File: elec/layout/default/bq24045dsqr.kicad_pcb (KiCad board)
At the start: 2 copper layers, 4 parts

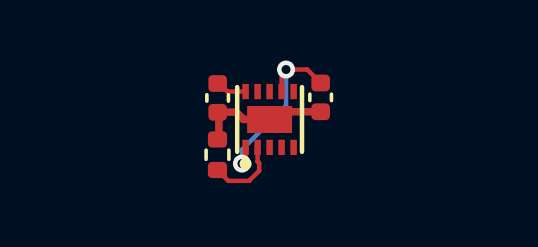
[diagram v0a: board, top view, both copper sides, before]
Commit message: updated to newest ato syntax, rearanged equations for solver
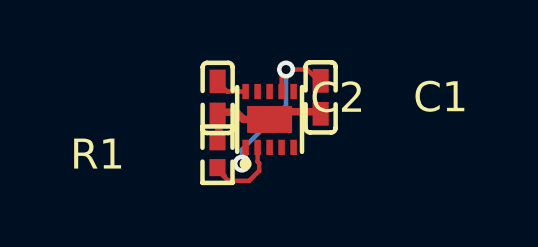
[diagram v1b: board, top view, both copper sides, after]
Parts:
- C1, C2: value 25V 1uF X5R ±10% 0402 Multilayer Ceramic Capacitors MLCC - SMD/SMT ROHS -> 1µF ±10% 25V X5R; footprint lib:C0402 -> atopile:C0402-b3ef17
- R1: value 100mW Thick Film Resistors ±100ppm/℃ ±1% 604Ω 0402 Chip Resistor - Surface Mount ROHS -> 560Ω ±1% 62.5mW; footprint lib:R0402 -> atopile:R0402-56259e
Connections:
- net chg renamed CHG
- net ic-gnd renamed gnd
- net ic-vcc renamed IN
- net ic-vcc-1 renamed OUT
- net iset renamed ISET
- net nc renamed NC
- net pg renamed PG
- net preterm renamed PRETERM
- net ts renamed TS
